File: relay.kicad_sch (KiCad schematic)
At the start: 5 parts, among them K1 Relay_SPST-NO, Q1 NMOS

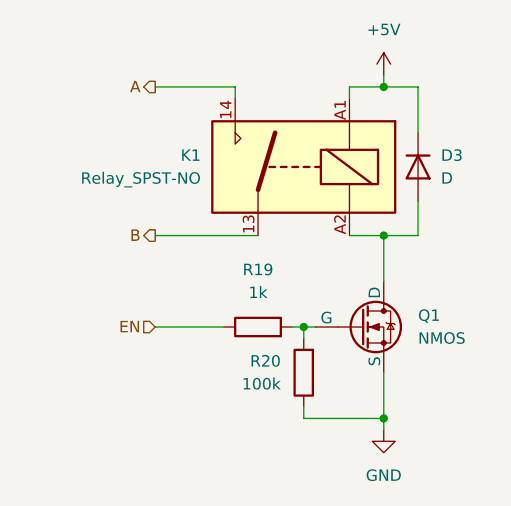
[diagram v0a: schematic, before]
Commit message: Assign footprints.
Signed-off-by: Dominik Bayerl <dominik.bayerl@carissma.eu>
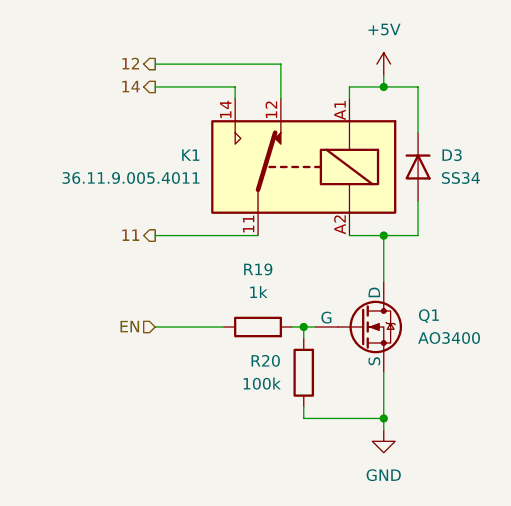
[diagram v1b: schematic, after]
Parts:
- removed K1: Relay_SPST-NO, symbol Relay:Relay_SPST-NO
- added K1: 36.11.9.005.4011, Relay_THT:Relay_SPDT_Finder_36.11, symbol Relay:Relay_SPDT
- D3: value D -> SS34; footprint Diode_SMD:D_SMC_Handsoldering -> Diode_SMD:D_SOD-123
- Q1: value NMOS -> AO3400
- R19, R20: footprint (none) -> Resistor_SMD:R_0603_1608Metric_Pad0.98x0.95mm_HandSolder
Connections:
- net +5V: now also K1.A1
- net at D3.2 (A), Q1.1 (D): now also K1.A2
- new net 11: K1.11
- new net 12: K1.12
- new net 14: K1.14
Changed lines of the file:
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@@
+	(wire
+		(pts
+			(xy 142.24 85.09) (xy 142.24 81.28)
+		)
+		(stroke
+			(width 0)
+			(type default)
+		)
+	)
 	(wire
 		(pts
@@
 	(wire
 		(pts
-			(xy 153.67 82.55) (xy 153.67 83.82)
+			(xy 142.24 81.28) (xy 128.27 81.28)
 		)
 		(stroke
@@
 		)
 	)
-	(hierarchical_label "B"
+	(wire
+		(pts
+			(xy 153.67 82.55) (xy 153.67 83.82)
+		)
+		(stroke
+			(width 0)
+			(type default)
+		)
+	)
+	(hierarchical_label "11"
 		(shape output)
 		(at 128.27 100.33 180)
@@
 		)
 	)
-	(hierarchical_label "A"
+	(hierarchical_label "12"
+		(shape output)
+		(at 128.27 81.28 180)
+		(effects
+			(font
+				(size 1.27 1.27)
+			)
+			(justify right)
+		)
+	)
+	(hierarchical_label "14"
 		(shape output)
 		(at 128.27 83.82 180)
@@
 			)
 			(justify right)
-		)
-	)
-	(symbol
-		(lib_id "Relay:Relay_SPST-NO")
-		(at 144.78 92.71 0)
-		(mirror y)
-		(unit 1)
-		(exclude_from_sim no)
-		(in_bom yes)
-		(on_board yes)
-		(dnp no)
-		(property "Reference" "K1"
-			(at 133.35 91.4399 0)
-			(effects
-				(font
-					(size 1.27 1.27)
-				)
-				(justify left)
-			)
-		)
-		(property "Value" "Relay_SPST-NO"
-			(at 133.35 93.9799 0)
-			(effects
-				(font
-					(size 1.27 1.27)
-				)
-				(justify left)
-			)
-		)
-		(property "Footprint" ""
-			(at 133.35 93.98 0)
-			(effects
-				(font
-					(size 1.27 1.27)
-				)
-				(justify left)
-				(hide yes)
-			)
-		)
-		(property "Datasheet" "~"
-			(at 144.78 92.71 0)
-			(effects
-				(font
-					(size 1.27 1.27)
-				)
-				(hide yes)
-			)
-		)
-		(property "Description" "Relay SPST, normally open, EN50005"
-			(at 144.78 92.71 0)
-			(effects
-				(font
-					(size 1.27 1.27)
-				)
-				(hide yes)
-			)
-		)
-		(pin "14"
-		)
-		(pin "A2"
-		)
-		(pin "13"
-		)
-		(pin "A1"
-		)
-		(instances
-			(project "esp32s3-rail"
-				(path "/43c3dd73-0dcc-48c9-a061-d039af0cb18f/3ad1b072-64e9-4e8d-a953-136ddf36af45"
-					(reference "K1")
-					(unit 1)
-				)
-				(path "/43c3dd73-0dcc-48c9-a061-d039af0cb18f/e67ace37-80ab-4353-9fe2-0a12de7a753d"
-					(reference "K2")
-					(unit 1)
-				)
-			)
 		)
 	)
@@
 			)
 		)
-		(property "Value" "NMOS"
+		(property "Value" "AO3400"
 			(at 157.48 111.7599 0)
 			(effects
@@
 		(instances
 			(project "esp32s3-rail"
-				(path "/43c3dd73-0dcc-48c9-a061-d039af0cb18f/3ad1b072-64e9-4e8d-a953-136ddf36af45"
+				(path "/43c3dd73-0dcc-48c9-a061-d039af0cb18f/0d2b1bd5-c022-4ed2-8a2f-3d2e0a748522"
 					(reference "Q1")
 					(unit 1)
@@
 			)
 		)
-		(property "Footprint" ""
+		(property "Footprint" "Resistor_SMD:R_0603_1608Metric_Pad0.98x0.95mm_HandSolder"
 			(at 139.7 112.268 90)
 			(effects
@@
 		(instances
 			(project "esp32s3-rail"
-				(path "/43c3dd73-0dcc-48c9-a061-d039af0cb18f/3ad1b072-64e9-4e8d-a953-136ddf36af45"
+				(path "/43c3dd73-0dcc-48c9-a061-d039af0cb18f/0d2b1bd5-c022-4ed2-8a2f-3d2e0a748522"
 					(reference "R19")
 					(unit 1)
@@
 				(path "/43c3dd73-0dcc-48c9-a061-d039af0cb18f/e67ace37-80ab-4353-9fe2-0a12de7a753d"
 					(reference "R27")
+					(unit 1)
+				)
+			)
+		)
+	)
+	(symbol
+		(lib_id "Relay:Relay_SPDT")
+		(at 144.78 92.71 0)
+		(mirror y)
+		(unit 1)
+		(exclude_from_sim no)
+		(in_bom yes)
+		(on_board yes)
+		(dnp no)
+		(property "Reference" "K1"
+			(at 133.35 91.4399 0)
+			(effects
+				(font
+					(size 1.27 1.27)
+				)
+				(justify left)
+			)
+		)
+		(property "Value" "36.11.9.005.4011"
+			(at 133.35 93.9799 0)
+			(effects
+				(font
+					(size 1.27 1.27)
+				)
+				(justify left)
+			)
+		)
+		(property "Footprint" "Relay_THT:Relay_SPDT_Finder_36.11"
+			(at 133.35 93.98 0)
+			(effects
+				(font
+					(size 1.27 1.27)
+				)
+				(justify left)
+				(hide yes)
+			)
+		)
+		(property "Datasheet" "~"
+			(at 144.78 92.71 0)
+			(effects
+				(font
+					(size 1.27 1.27)
+				)
+				(hide yes)
+			)
+		)
+		(property "Description" "Relay SPDT, monostable, EN50005"
+			(at 144.78 92.71 0)
+			(effects
+				(font
+					(size 1.27 1.27)
+				)
+				(hide yes)
+			)
+		)
+		(pin "A1"
+		)
+		(pin "14"
+		)
+		(pin "12"
+		)
+		(pin "11"
+		)
+		(pin "A2"
+		)
+		(instances
+			(project "esp32s3-rail"
+				(path "/43c3dd73-0dcc-48c9-a061-d039af0cb18f/0d2b1bd5-c022-4ed2-8a2f-3d2e0a748522"
+					(reference "K1")
+					(unit 1)
+				)
+				(path "/43c3dd73-0dcc-48c9-a061-d039af0cb18f/e67ace37-80ab-4353-9fe2-0a12de7a753d"
+					(reference "K2")
 					(unit 1)
 				)
@@
 		(instances
 			(project "esp32s3-rail"
-				(path "/43c3dd73-0dcc-48c9-a061-d039af0cb18f/3ad1b072-64e9-4e8d-a953-136ddf36af45"
+				(path "/43c3dd73-0dcc-48c9-a061-d039af0cb18f/0d2b1bd5-c022-4ed2-8a2f-3d2e0a748522"
 					(reference "#PWR054")
 					(unit 1)
@@
 			)
 		)
-		(property "Footprint" ""
+		(property "Footprint" "Resistor_SMD:R_0603_1608Metric_Pad0.98x0.95mm_HandSolder"
 			(at 146.558 115.57 90)
 			(effects
@@
 		(instances
 			(project "esp32s3-rail"
-				(path "/43c3dd73-0dcc-48c9-a061-d039af0cb18f/3ad1b072-64e9-4e8d-a953-136ddf36af45"
+				(path "/43c3dd73-0dcc-48c9-a061-d039af0cb18f/0d2b1bd5-c022-4ed2-8a2f-3d2e0a748522"
 					(reference "R20")
 					(unit 1)
@@
 		(instances
 			(project "esp32s3-rail"
-				(path "/43c3dd73-0dcc-48c9-a061-d039af0cb18f/3ad1b072-64e9-4e8d-a953-136ddf36af45"
+				(path "/43c3dd73-0dcc-48c9-a061-d039af0cb18f/0d2b1bd5-c022-4ed2-8a2f-3d2e0a748522"
 					(reference "#PWR055")
 					(unit 1)
@@
 			)
 		)
-		(property "Value" "D"
+		(property "Value" "SS34"
 			(at 160.02 93.9799 90)
 			(effects
@@
 			)
 		)
-		(property "Footprint" "Diode_SMD:D_SMC_Handsoldering"
+		(property "Footprint" "Diode_SMD:D_SOD-123"
 			(at 157.48 92.71 0)
 			(effects
@@
 		(instances
 			(project "esp32s3-rail"
-				(path "/43c3dd73-0dcc-48c9-a061-d039af0cb18f/3ad1b072-64e9-4e8d-a953-136ddf36af45"
+				(path "/43c3dd73-0dcc-48c9-a061-d039af0cb18f/0d2b1bd5-c022-4ed2-8a2f-3d2e0a748522"
 					(reference "D3")
 					(unit 1)
